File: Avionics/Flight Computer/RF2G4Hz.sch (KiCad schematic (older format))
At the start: 35 parts, among them J5 0734120110, U3 CC2650F128RGZR, U4 CC2592RGVR, Y5 XRCGB24M000F2P00R0

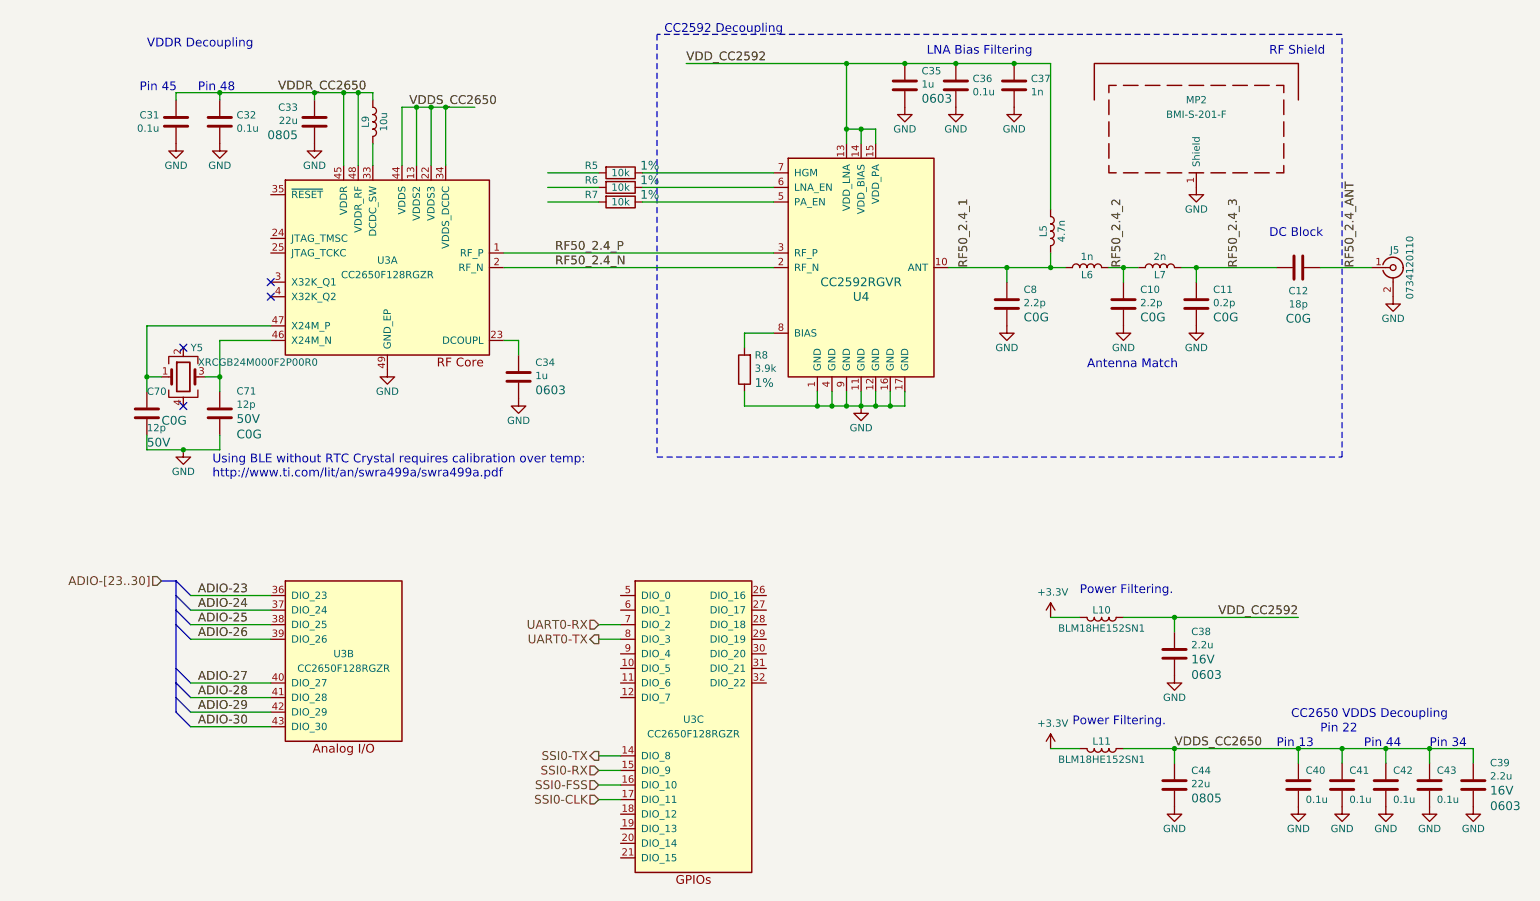
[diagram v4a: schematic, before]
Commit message: Added additional pinout
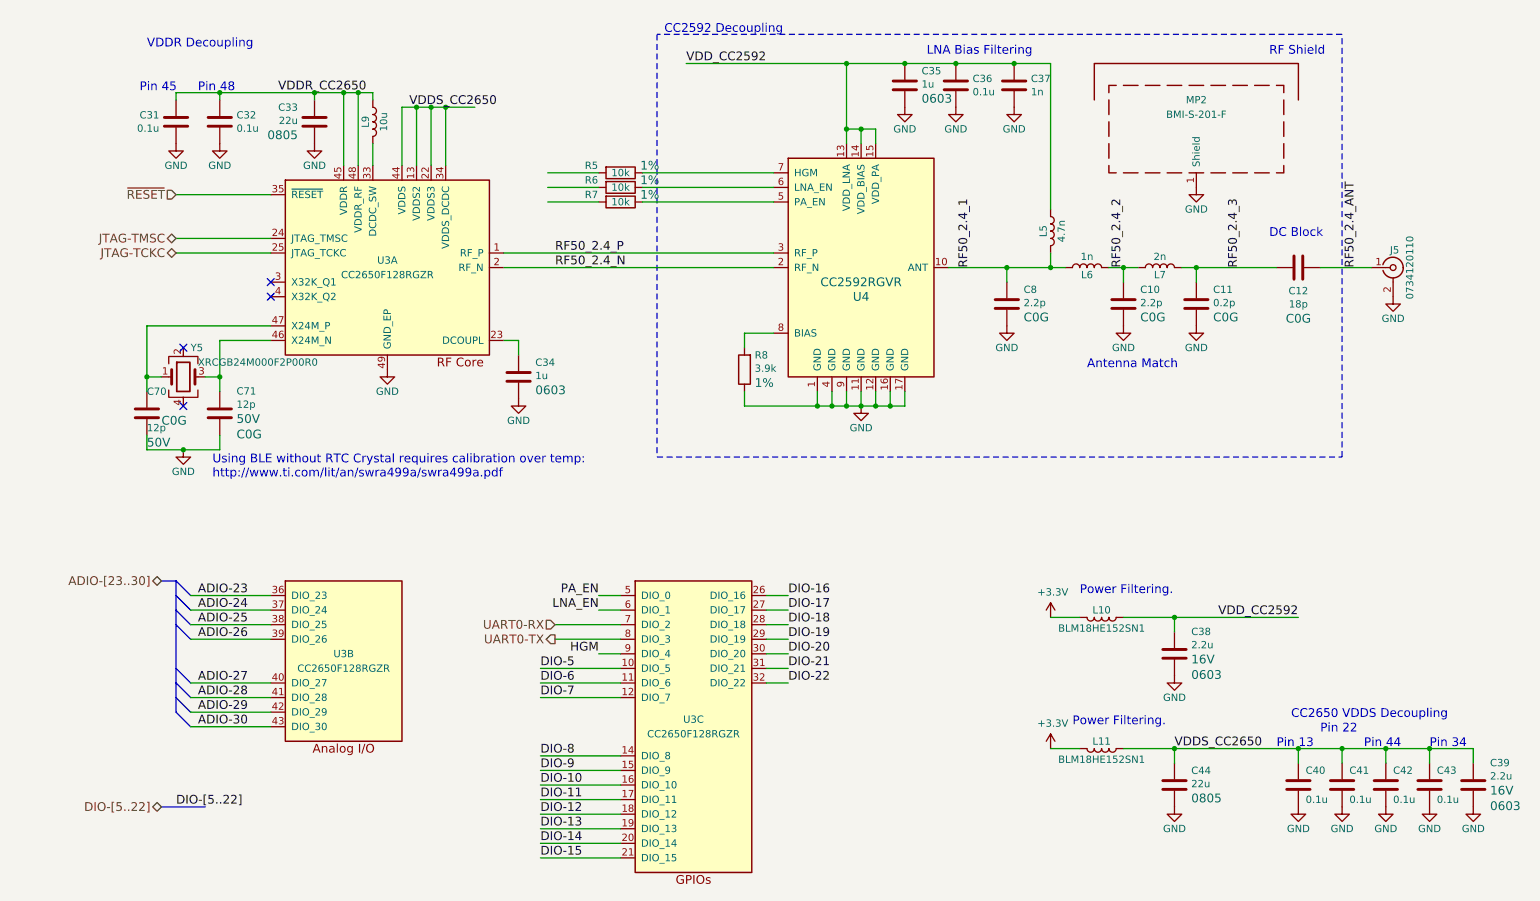
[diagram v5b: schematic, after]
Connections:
- net labels added: DIO-10, DIO-11, DIO-12, DIO-13, DIO-14, DIO-15, DIO-16, DIO-17, DIO-18, DIO-19, DIO-20, DIO-21, DIO-22, DIO-5, DIO-6, DIO-7, DIO-8, DIO-9, DIO-[5..22], HGM, JTAG-TCKC, JTAG-TMSC, LNA_EN, PA_EN, ~RESET
- net labels removed: SSI0-CLK, SSI0-FSS, SSI0-RX, SSI0-TX
- wire segments 82 -> 102

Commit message: Wired up everything and started rearranging layout
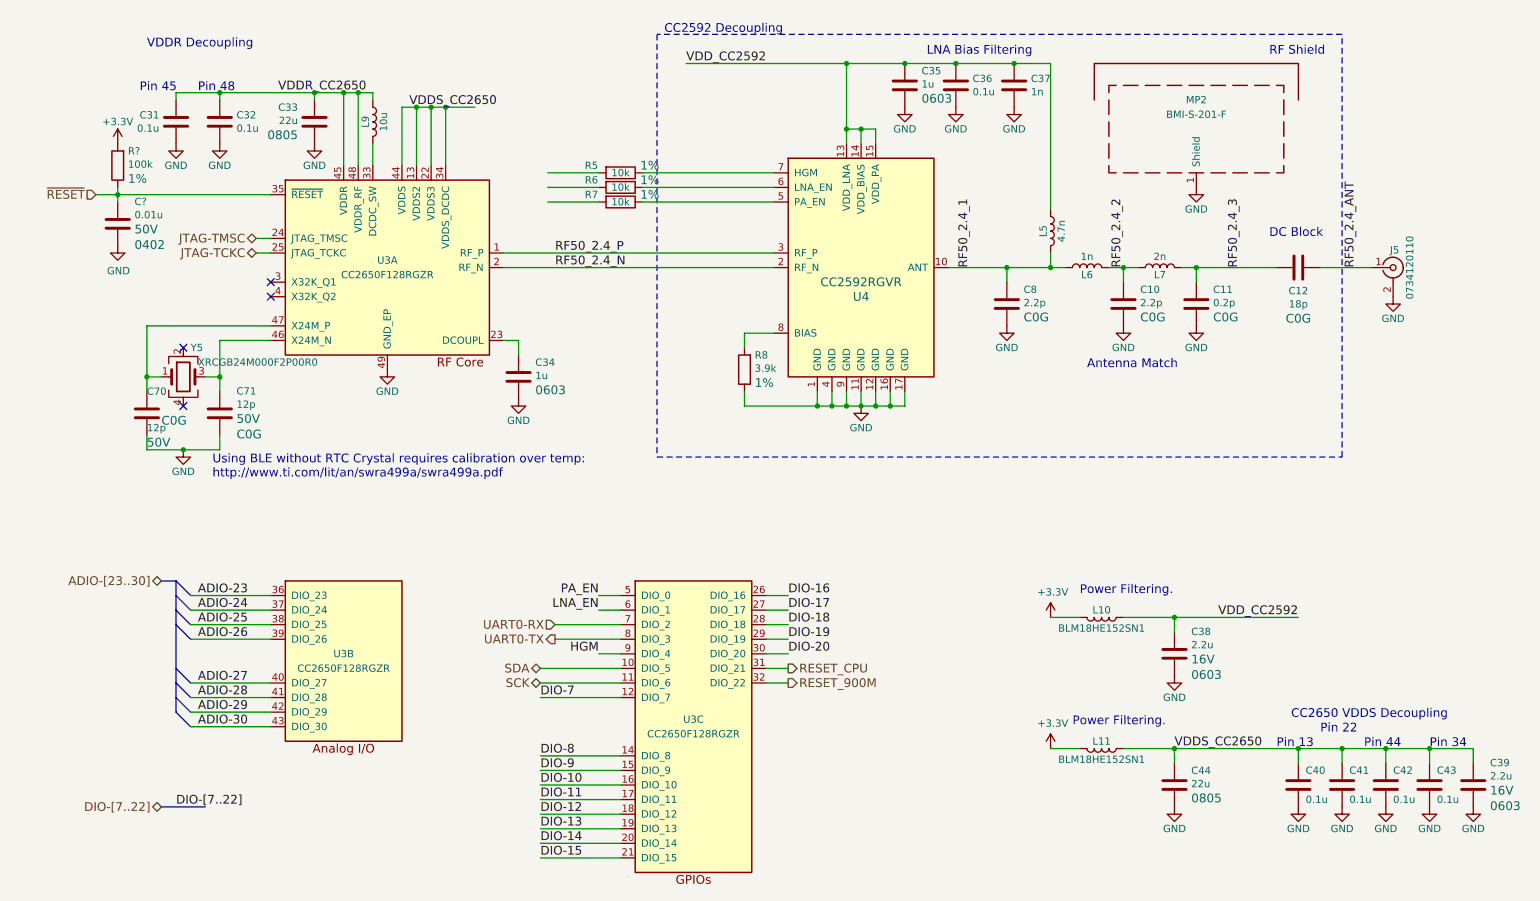
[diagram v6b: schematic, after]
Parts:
- added C?: 0.01u, Capacitors_SMD:C_0402, symbol C
- added R?: 100k, Resistors_SMD:R_0402, symbol R
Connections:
- net labels added: DIO-[7..22], RESET_900M, RESET_CPU, SCK, SDA
- net labels removed: DIO-21, DIO-22, DIO-5, DIO-6, DIO-[5..22]
- wire segments 102 -> 137
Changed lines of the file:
@@
 $Descr A4 11693 8268
 encoding utf-8
-Sheet 4 9
+Sheet 4 8
 Title ""
 Date ""
@@
 Text HLabel 1300 4450 0    60   BiDi ~ 0
 ADIO-[23..30]
-Text Label 3900 5050 0    60   ~ 0
-DIO-5
 Text Label 1550 4650 0    60   ~ 0
 ADIO-24
@@
 	9250 2300 9600 2300
 Wire Wire Line
-	8300 2300 8950 2300
+	8300 2300 8400 2300
+Wire Wire Line
+	8400 2300 8950 2300
 Wire Wire Line
 	8400 2400 8400 2300
 Connection ~ 8400 2300
 Wire Wire Line
-	7800 2300 8000 2300
+	7800 2300 7900 2300
+Wire Wire Line
+	7900 2300 8000 2300
 Wire Wire Line
 	7900 2400 7900 2300
 Connection ~ 7900 2300
 Wire Wire Line
-	6700 2300 7500 2300
+	6700 2300 7100 2300
+Wire Wire Line
+	7100 2300 7400 2300
+Wire Wire Line
+	7400 2300 7500 2300
 Wire Wire Line
 	7400 2300 7400 2200
@@
 	7400 900  7400 1900
 Wire Wire Line
-	7900 4700 9100 4700
-Wire Wire Line
-	6000 900  6000 1450
+	7900 4700 8250 4700
+Wire Wire Line
+	8250 4700 9100 4700
+Wire Wire Line
+	6000 900  6000 1350
+Wire Wire Line
+	6000 1350 6000 1450
 Wire Wire Line
 	6100 1450 6100 1350
 Wire Wire Line
-	6000 1350 6200 1350
+	6000 1350 6100 1350
+Wire Wire Line
+	6100 1350 6200 1350
 Connection ~ 6000 1350
 Wire Wire Line
@@
 	7400 4700 7600 4700
 Wire Wire Line
-	7900 5600 10300 5600
+	7900 5600 8250 5600
+Wire Wire Line
+	8250 5600 9100 5600
+Wire Wire Line
+	9100 5600 9400 5600
+Wire Wire Line
+	9400 5600 9700 5600
+Wire Wire Line
+	9700 5600 10000 5600
+Wire Wire Line
+	10000 5600 10300 5600
 Wire Wire Line
 	7400 5600 7600 5600
 Wire Wire Line
-	5300 3250 6400 3250
+	5300 3250 5800 3250
+Wire Wire Line
+	5800 3250 5900 3250
+Wire Wire Line
+	5900 3250 6000 3250
+Wire Wire Line
+	6000 3250 6100 3250
+Wire Wire Line
+	6100 3250 6200 3250
+Wire Wire Line
+	6200 3250 6300 3250
+Wire Wire Line
+	6300 3250 6400 3250
 Wire Wire Line
 	5800 3250 5800 3150
@@
 	2550 1100 2550 1600
 Wire Wire Line
-	1400 1100 2750 1100
+	1400 1100 1700 1100
+Wire Wire Line
+	1700 1100 2350 1100
+Wire Wire Line
+	2350 1100 2550 1100
+Wire Wire Line
+	2550 1100 2650 1100
+Wire Wire Line
+	2650 1100 2750 1100
 Wire Wire Line
 	2750 1100 2750 1150
@@
 	2950 1600 2950 1200
 Wire Wire Line
-	2950 1200 3450 1200
+	2950 1200 3050 1200
+Wire Wire Line
+	3050 1200 3150 1200
+Wire Wire Line
+	3150 1200 3250 1200
+Wire Wire Line
+	3250 1200 3450 1200
 Wire Wire Line
 	3250 1200 3250 1600
@@
 Connection ~ 8250 5600
 Wire Wire Line
-	4900 900  7400 900
+	4900 900  6000 900
+Wire Wire Line
+	6000 900  6400 900
+Wire Wire Line
+	6400 900  6750 900
+Wire Wire Line
+	6750 900  7150 900
+Wire Wire Line
+	7150 900  7400 900
 Connection ~ 6400 900
 Connection ~ 6750 900
@@
 	1200 3450 1200 3550
 Wire Wire Line
-	1200 3550 1700 3550
+	1200 3550 1450 3550
+Wire Wire Line
+	1450 3550 1700 3550
 Wire Wire Line
 	1700 3550 1700 3450
@@
 	1300 3050 1200 3050
 Wire Wire Line
-	1200 2700 1200 3150
+	1200 2700 1200 3050
+Wire Wire Line
+	1200 3050 1200 3150
 Wire Wire Line
 	1600 3050 1700 3050
 Wire Wire Line
-	1700 2800 1700 3150
+	1700 2800 1700 3050
+Wire Wire Line
+	1700 3050 1700 3150
 Wire Wire Line
 	1700 2800 2050 2800
@@
 	4000 4850 4450 4850
 Wire Bus Line
-	1400 4450 1400 5350
+	1400 4450 1400 4550
+Wire Bus Line
+	1400 4550 1400 4650
+Wire Bus Line
+	1400 4650 1400 4750
+Wire Bus Line
+	1400 4750 1400 5050
+Wire Bus Line
+	1400 5050 1400 5150
+Wire Bus Line
+	1400 5150 1400 5250
+Wire Bus Line
+	1400 5250 1400 5350
 Wire Bus Line
 	1400 4450 1300 4450
@@
 Wire Wire Line
 	3900 5050 4450 5050
-Text Label 3900 5150 0    60   ~ 0
-DIO-6
 Text Label 3900 5250 0    60   ~ 0
 DIO-7
@@
 Text Label 5600 4950 0    60   ~ 0
 DIO-20
-Text Label 5600 5050 0    60   ~ 0
-DIO-21
-Text Label 5600 5150 0    60   ~ 0
-DIO-22
 Wire Wire Line
 	5450 5150 5600 5150
@@
 	5450 4550 5600 4550
 Text HLabel 1300 6000 0    60   BiDi ~ 0
-DIO-[5..22]
+DIO-[7..22]
 Wire Bus Line
 	1300 6000 1600 6000
 Text Label 1400 6000 0    60   ~ 0
-DIO-[5..22]
+DIO-[7..22]
 Wire Wire Line
 	1500 4550 2050 4550
 Text Label 1550 4550 0    60   ~ 0
 ADIO-23
-Text HLabel 1400 1800 0    60   Input ~ 0
+Text HLabel 850  1800 0    60   Input ~ 0
 ~RESET
 Wire Wire Line
-	1400 1800 2050 1800
-Wire Wire Line
-	1400 2100 2050 2100
-Wire Wire Line
-	1400 2200 2050 2200
-Text HLabel 1400 2100 0    60   BiDi ~ 0
+	850  1800 1000 1800
+Wire Wire Line
+	1000 1800 2050 1800
+Wire Wire Line
+	1950 2100 2050 2100
+Wire Wire Line
+	1950 2200 2050 2200
+Text HLabel 1950 2100 0    60   BiDi ~ 0
 JTAG-TMSC
-Text HLabel 1400 2200 0    60   BiDi ~ 0
+Text HLabel 1950 2200 0    60   BiDi ~ 0
 JTAG-TCKC
+Text HLabel 3900 5050 0    60   BiDi ~ 0
+SDA
+Text HLabel 3900 5150 0    60   BiDi ~ 0
+SCK
+Text HLabel 5600 5050 2    60   Output ~ 0
+RESET_CPU
+Text HLabel 5600 5150 2    60   Output ~ 0
+RESET_900M
+$Comp
+L C C?
+U 1 1 58C2804F
+P 1000 2000
+F 0 "C?" H 1115 2152 50  0000 L CNN
+F 1 "0.01u" H 1115 2061 50  0000 L CNN
+F 2 "Capacitors_SMD:C_0402" H -4712 -850 50  0001 C CNN
+F 3 "" H -4750 -700 50  0001 C CNN
+F 4 "50V" H 1115 1962 60  0000 L CNN "Voltage"
+F 5 "20%" H 1115 1909 60  0001 L CNN "Tolerance"
+F 6 "X7R" H 1115 1856 60  0001 L CNN "Type"
+F 7 "0402" H 1115 1856 60  0000 L CNN "Package"
+	1    1000 2000
+	1    0    0    -1
+$EndComp
+$Comp
+L GND #PWR?
+U 1 1 58C28056
+P 1000 2150
+F 0 "#PWR?" H 1050 2200 50  0001 C CNN
+F 1 "GND" H 1005 1977 50  0000 C CNN
+F 2 "" H -5800 -1600 50  0001 C CNN
+F 3 "" H -5800 -1600 50  0001 C CNN
+	1    1000 2150
+	1    0    0    -1
+$EndComp
+Wire Wire Line
+	1000 1750 1000 1800
+Wire Wire Line
+	1000 1800 1000 1850
+Connection ~ 1000 1800
+$Comp
+L R R?
+U 1 1 58C2935E
+P 1000 1600
+F 0 "R?" H 930 1501 50  0000 R CNN
+F 1 "100k" H 930 1592 50  0000 R CNN
+F 2 "Resistors_SMD:R_0402" V -4000 300 50  0001 C CNN
+F 3 "" V -3720 300 50  0001 C CNN
+F 4 "1%" H 930 1691 60  0000 R CNN "Tolerance"
+F 5 "50V" V -3550 300 60  0001 C CNN "Voltage"
+F 6 "0.062W" V -3450 300 60  0001 C CNN "Power"
+F 7 "Thin Film" V -3350 300 60  0001 C CNN "Material"
+F 8 "0402" V -3900 300 60  0001 C CNN "Package"
+	1    1000 1600
+	-1   0    0    1
+$EndComp
+$Comp
+L +3.3V #PWR?
+U 1 1 58C2A4C4
+P 1000 1450
+F 0 "#PWR?" H 1050 1500 50  0001 C CNN
+F 1 "+3.3V" H 1000 1600 50  0000 C CNN
+F 2 "" H -6350 -3350 50  0001 C CNN
+F 3 "" H -6350 -3350 50  0001 C CNN
+	1    1000 1450
+	1    0    0    -1
+$EndComp
 $EndSCHEMATC

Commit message: Finished breaking out signals to connector sheet and interconnecting processors.
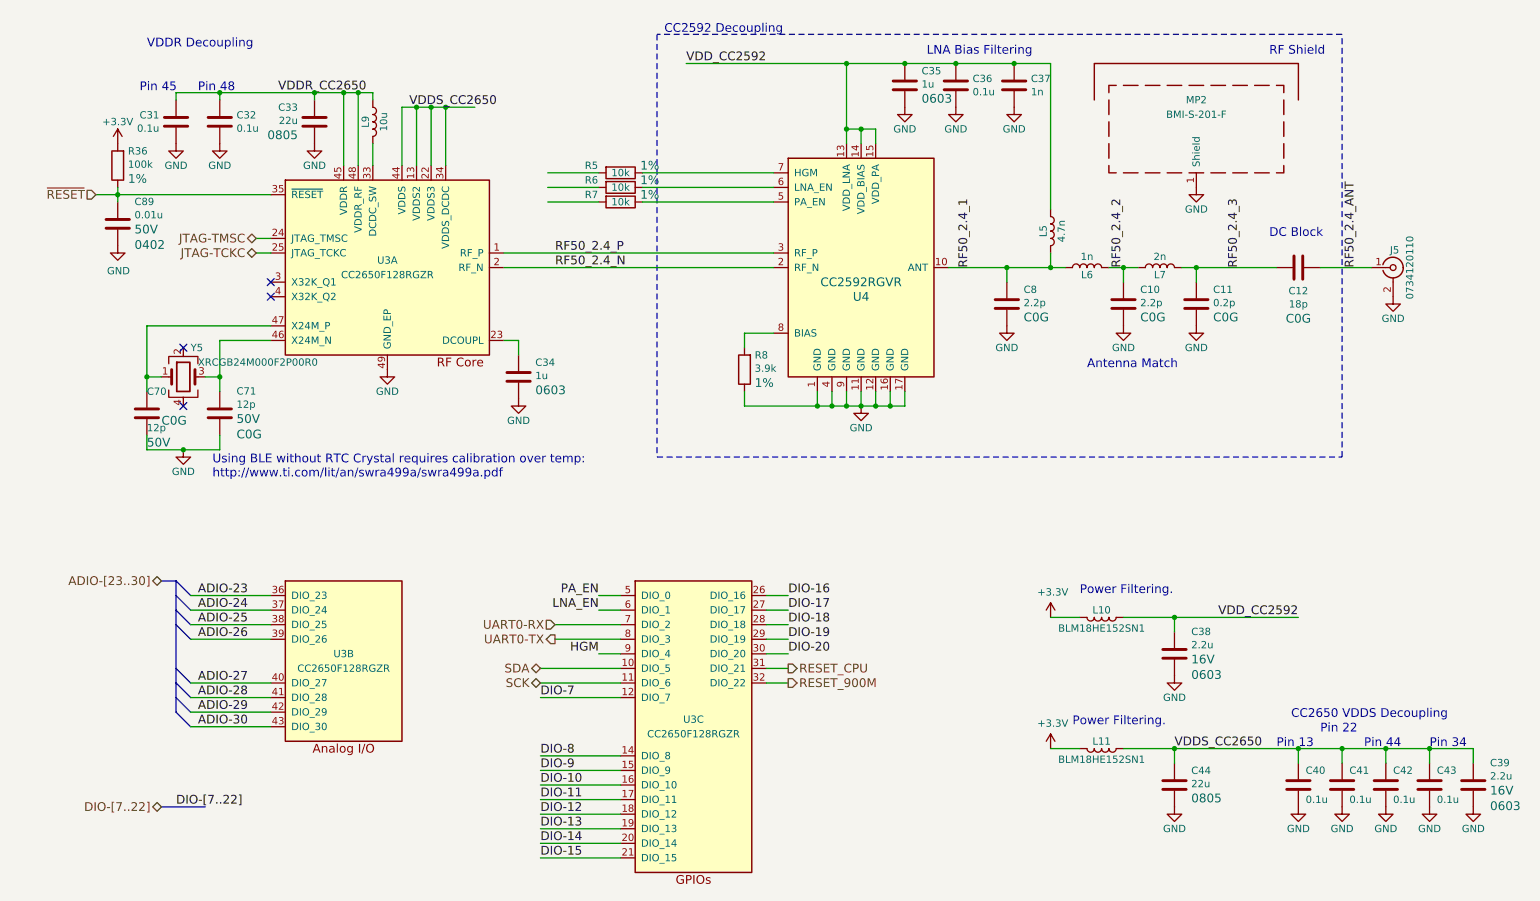
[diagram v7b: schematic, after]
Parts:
- gave numbers to parts that had none: 2
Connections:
- wire segments 137 -> 103

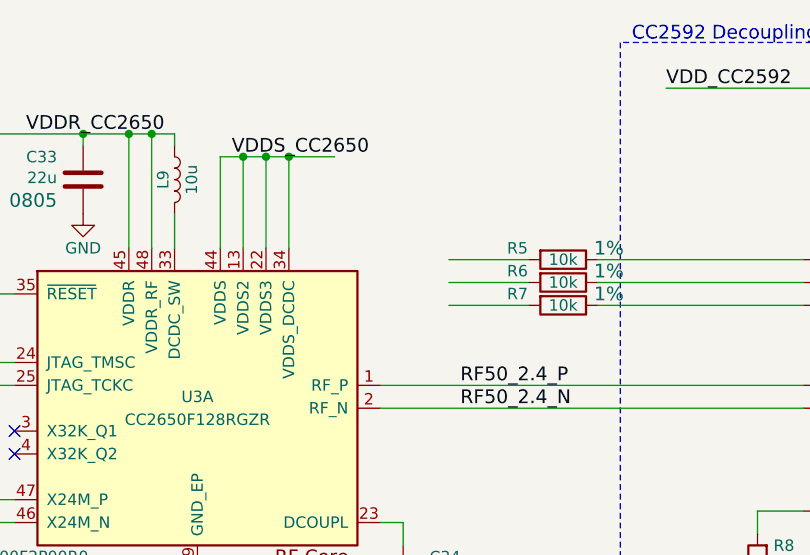
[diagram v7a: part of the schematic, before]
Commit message: Fixed missing connections and did more layout
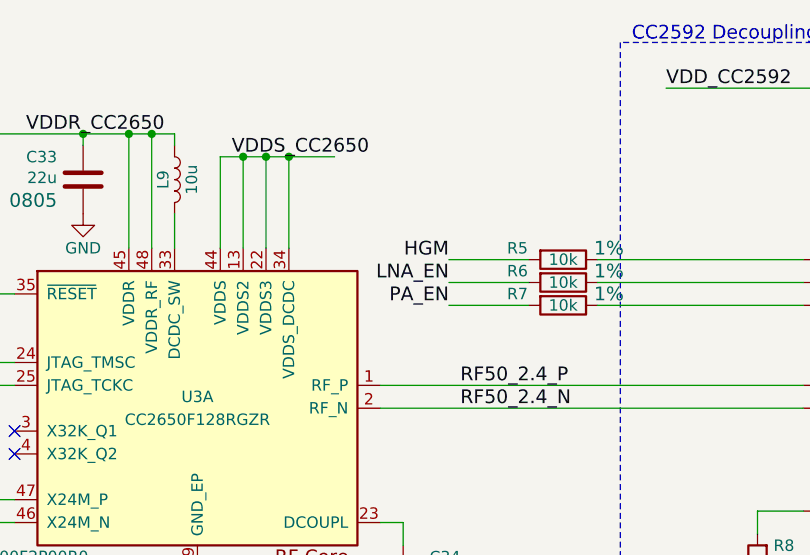
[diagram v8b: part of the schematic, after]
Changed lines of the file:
@@
 	1    0    0    -1
 $EndComp
+Text Label 3950 1850 2    60   ~ 0
+PA_EN
+Text Label 3950 1750 2    60   ~ 0
+LNA_EN
+Text Label 3950 1650 2    60   ~ 0
+HGM
 $EndSCHEMATC
